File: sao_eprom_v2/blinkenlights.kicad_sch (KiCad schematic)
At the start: 9 parts

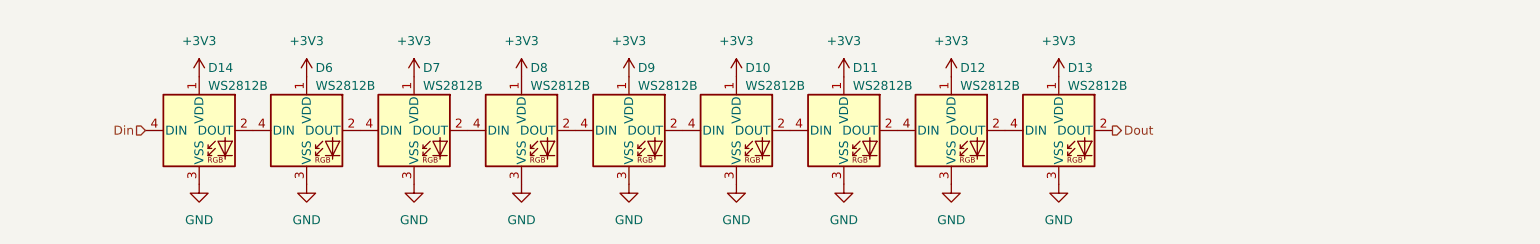
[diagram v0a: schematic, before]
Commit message: Now with QWIIC and TestPads!
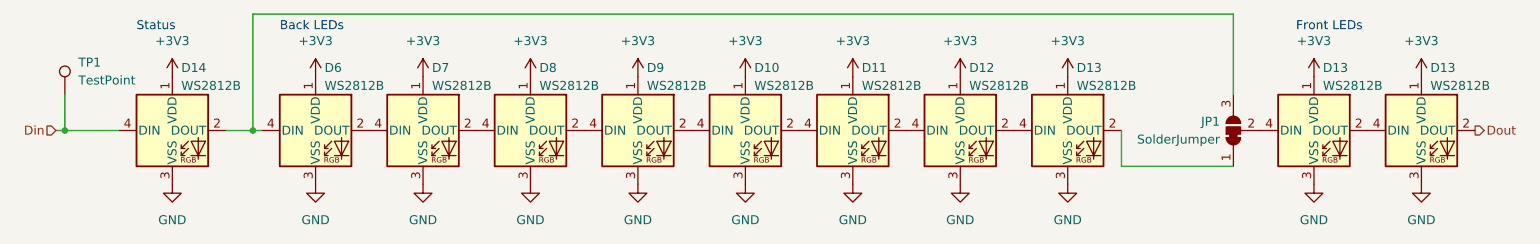
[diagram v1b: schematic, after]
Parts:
- added D13 (x2): WS2812B, LED_SMD:LED_WS2812B_PLCC4_5.0x5.0mm_P3.2mm, symbol LED:WS2812B
- added JP1: SolderJumper, Jumper:SolderJumper-3_P1.3mm_Bridged2Bar12_Pad1.0x1.5mm, symbol Jumper:SolderJumper_3_Bridged12
- added TP1: TestPoint, TestPoint:TestPoint_Pad_D1.0mm, symbol Connector:TestPoint
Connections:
- net +3V3: now also D13.1 (VDD), D13.1 (VDD)
- net Din: now also TP1.1
- net Dout: now also D13.2 (DOUT); no longer D13.2 (DOUT)
- net GND: now also D13.3 (VSS), D13.3 (VSS)
- net at D14.2 (DOUT), D6.4 (DIN): now also JP1.3 (B)
- new net: D13.2 (DOUT), JP1.1 (A)
- new net: D13.4 (DIN), JP1.2 (C)
- new net: D13.2 (DOUT), D13.4 (DIN)
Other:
- note added: "Back LEDs"
- note added: "Front LEDs"
- note added: "Status"
- moved on the sheet: D10, D11, D12, D13, D14, D6, D7, D8, D9
